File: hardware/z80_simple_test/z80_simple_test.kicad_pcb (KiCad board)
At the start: 2 copper layers, 95 x 100 mm, 38 parts, among them J2 Conn_02x15_Odd_Even, U1 Z84C000XPEG, U2 SRAM_512K8B_DIP_SOP_SOJ, U3 EEPROM_512K8B_DIP, U4 74XX138, U5 Z84C200XPEG, U6 Z84C200XPEG

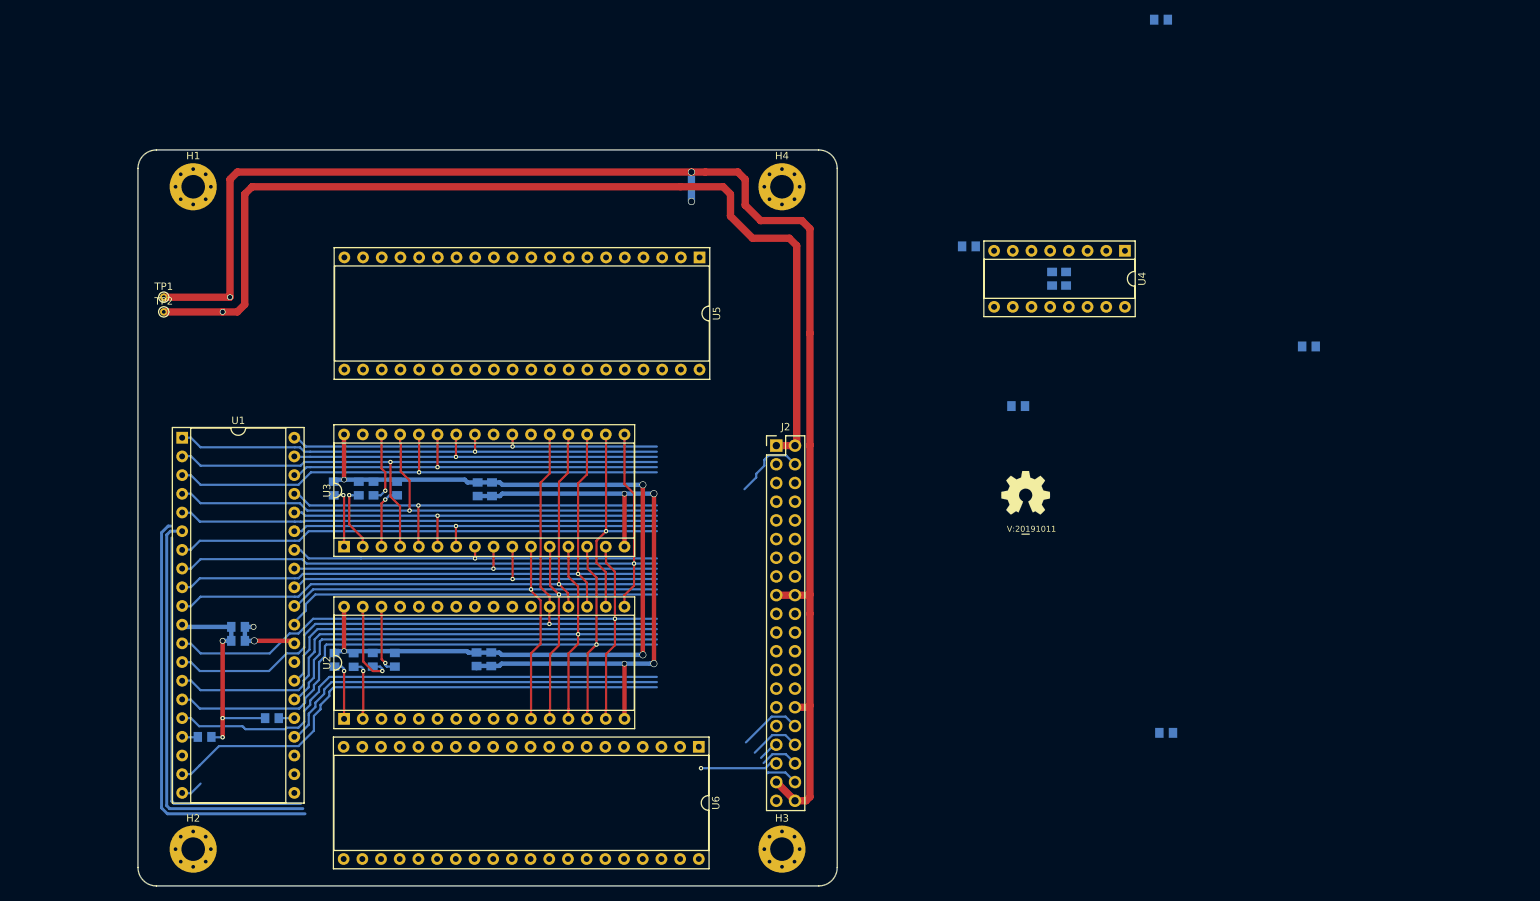
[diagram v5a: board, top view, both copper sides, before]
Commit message: after a bunch of false starts, this bus setup seems workable
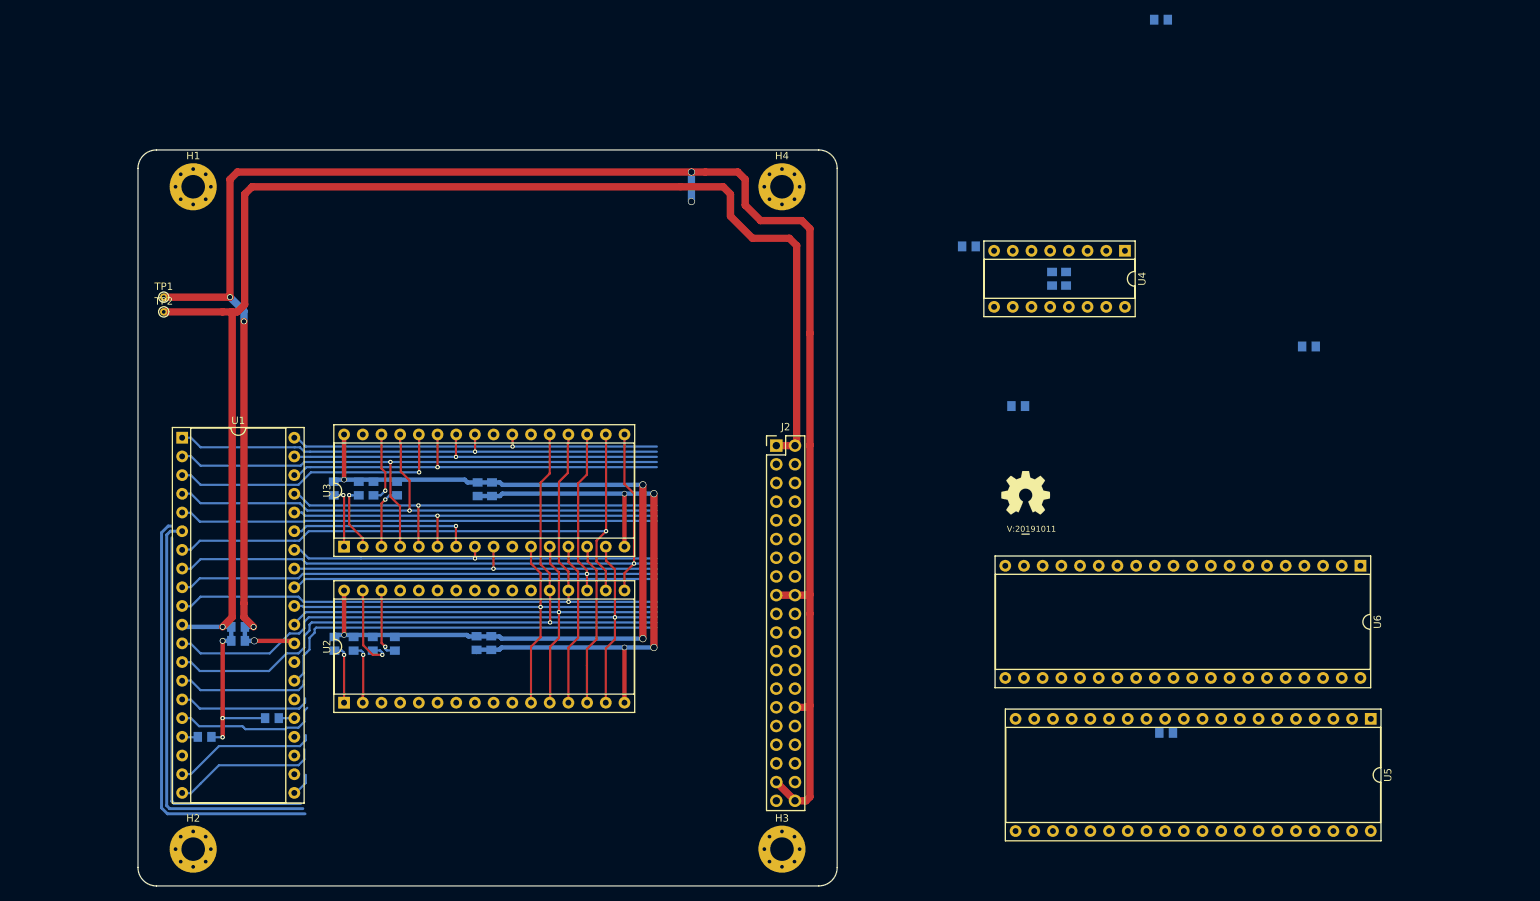
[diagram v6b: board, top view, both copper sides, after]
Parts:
- moved U5 110.7 mm to (270.0, 127.3)
- moved U6 93.2 mm to (268.6, 106.5)
- moved C3 2.20 mm to (148.5, 117.0)
- moved C4 2.20 mm to (150.5, 117.0)
- moved R4 2.20 mm to (131.8, 117.1)
- moved U2 2.20 mm to (130.5, 125.1)
- moved R5 2.18 mm to (129.2, 117.1)
- moved R6 2.18 mm to (137.4, 117.1)
- moved R7 2.18 mm to (134.4, 117.1)
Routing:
- net /!RESET: track 64.0 -> 0.30 mm
- net /!MREQ: track 78.3 -> 19.4 mm
- net /!WAIT: track 56.7 -> 0.32 mm
- net /D1: track 96.0 -> 40.4 mm, vias 1 -> 0
- net /D0: track 95.4 -> 40.2 mm, vias 1 -> 0
- net /!INT: track 69.6 -> 19.7 mm
- net /VSS: track 412.3 -> 456.2 mm, vias 9 -> 10
- net /VDD: track 286.9 -> 328.1 mm
- net /A13: track 70.9 -> 38.6 mm
- net /A5: track 52.4 -> 25.1 mm
- net /A15: track 75.1 -> 65.1 mm
- net /D4: track 90.0 -> 80.9 mm
- net /!IORQ: track 13.6 -> 19.9 mm, vias 1 -> 0
- net /!WR: track 5.82 -> 1.18 mm
- net /A2: track 54.1 -> 49.8 mm, vias 1 -> 0
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
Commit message: added zilog SIO to schematic and PCB
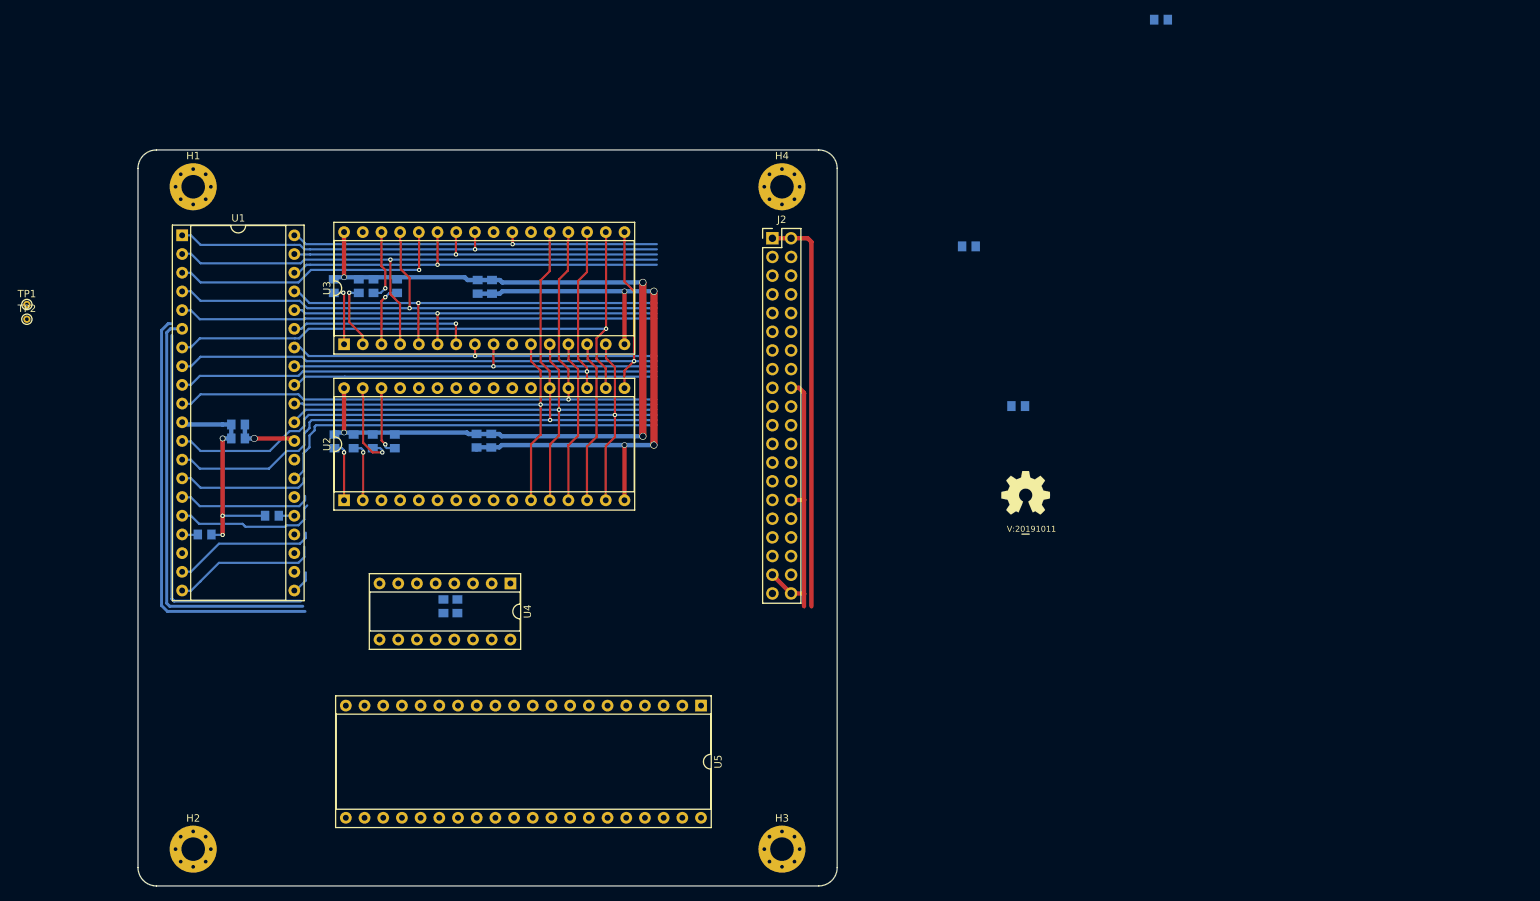
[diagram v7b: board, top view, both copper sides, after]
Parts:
- removed C11: 100n, SquantorRcl:C_0805+0603
- removed C12: 1u, SquantorRcl:C_0805+0603
- removed U6: Z84C200XPEG, Package_DIP:DIP-40_W15.24mm_Socket
- U5: value Z84C200XPEG -> Z84C40XPEG
- moved U4 94.9 mm to (153.1, 108.9)
- moved C7 93.9 mm to (144.0, 112.0)
- moved C8 93.9 mm to (145.9, 112.0)
- moved U5 91.0 mm to (179.0, 125.5)
- moved J2 28.2 mm to (188.7, 62.0)
- moved C1 27.5 mm to (116.1, 87.3)
- moved C2 27.5 mm to (116.1, 89.2)
- moved C3 27.5 mm to (148.5, 89.5)
- moved C4 27.5 mm to (150.5, 89.5)
- moved C5 27.5 mm to (150.6, 68.6)
- moved C6 27.5 mm to (148.7, 68.6)
- moved R1 27.5 mm to (120.7, 99.7)
- moved R10 27.5 mm to (134.5, 68.5)
- moved R11 27.5 mm to (129.1, 68.5)
- moved R3 27.5 mm to (111.5, 102.2)
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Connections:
- J2 pad 17: /VSS -> /A1
- J2 pad 19: /A0 -> /D7
- J2 pad 20: /A1 -> /A0
- J2 pad 21: /D6 -> /D5
- J2 pad 22: /D7 -> /D6
- J2 pad 23: /D4 -> /D3
- J2 pad 24: /D5 -> /D4
- J2 pad 25: /D2 -> /D1
- J2 pad 26: /D3 -> /D2
- J2 pad 27: /D0 -> /!IEI
- J2 pad 28: /D1 -> /D0
- U4 pad 14: (no net) -> /SEL_SIO
- U5 pad 1: /D2 -> /D1
- U5 pad 11: /VSS -> (no net)
- U5 pad 19: /D0 -> (no net)
- U5 pad 2: /D7 -> /D3
- U5 pad 20: /D1 -> /MCLK
- U5 pad 21: (no net) -> /!RESET
- U5 pad 23: /!INT -> (no net)
- U5 pad 25: /MCLK -> (no net)
- U5 pad 26: /VDD -> (no net)
- U5 pad 3: /D6 -> /D5
- U5 pad 31: (no net) -> /VSS
- U5 pad 32: (no net) -> /!RD
- U5 pad 33: (no net) -> /A1
- U5 pad 34: (no net) -> /A0
- U5 pad 35: /!RD -> /SEL_SIO
- U5 pad 37: /!M1 -> /D6
- U5 pad 38: /D5 -> /D4
- U5 pad 39: /D4 -> /D2
- U5 pad 4: /SEL_PIO -> /D7
- U5 pad 40: /D3 -> /D0
- U5 pad 5: /A1 -> /!INT
- U5 pad 6: /A0 -> /!IEI
- U5 pad 8: (no net) -> /!M1
- U5 pad 9: (no net) -> /VDD
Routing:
- net /VSS: track 456.2 -> 243.3 mm, vias 10 -> 5
- net /VDD: track 328.1 -> 203.0 mm, vias 8 -> 7

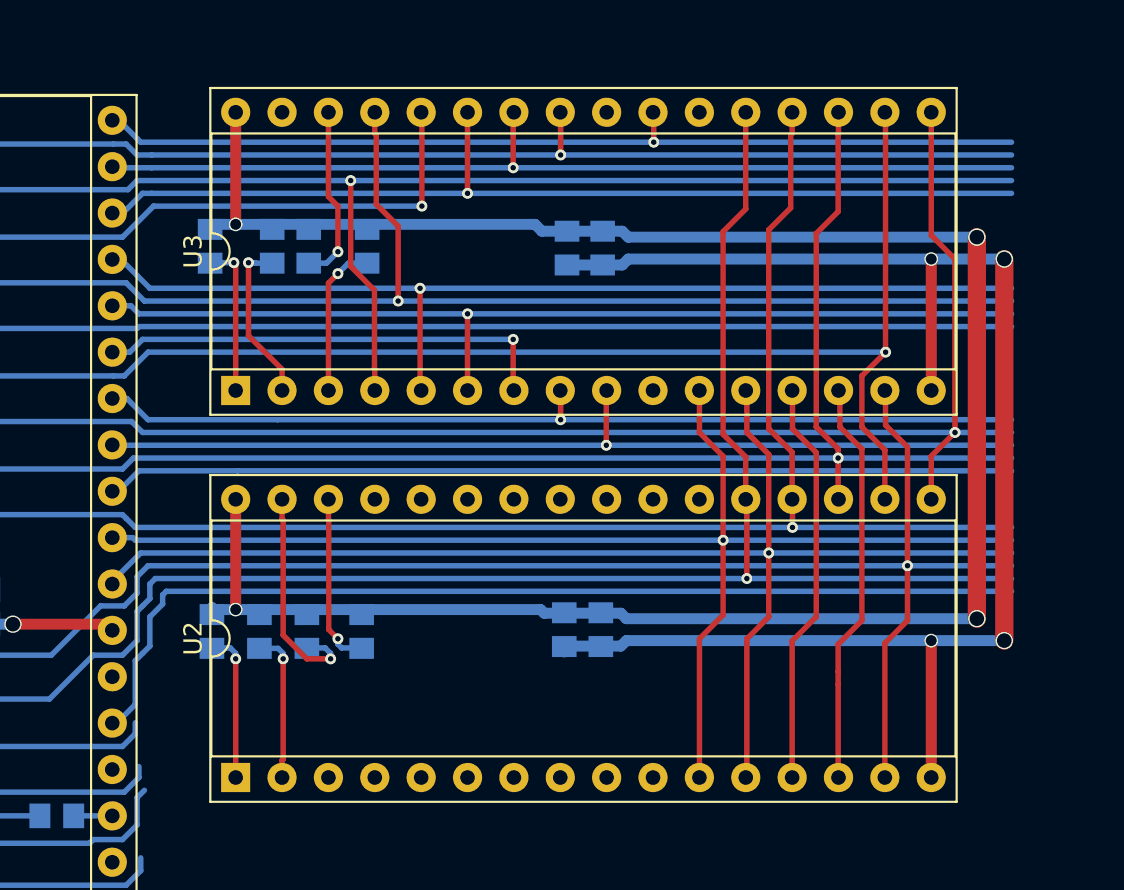
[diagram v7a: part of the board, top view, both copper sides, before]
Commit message: routed bus under memory chips
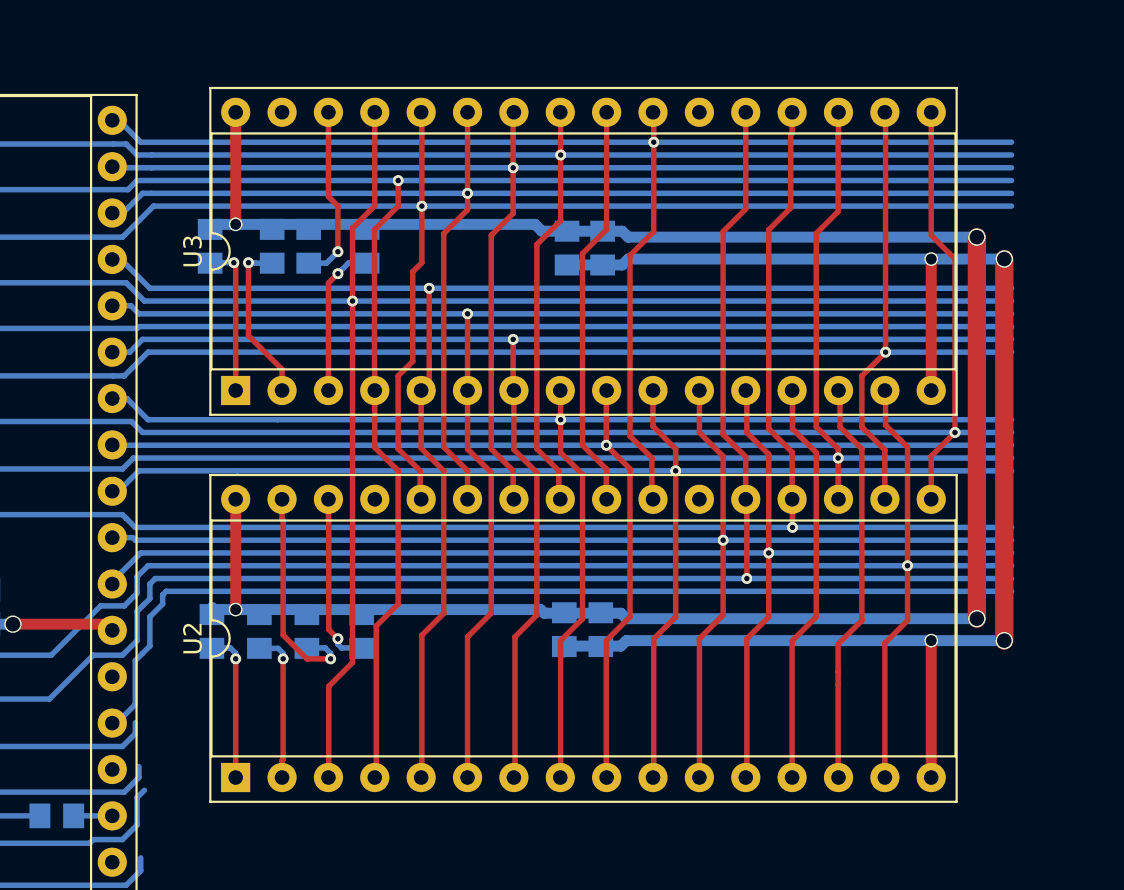
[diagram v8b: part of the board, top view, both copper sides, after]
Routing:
- net /A5: track 25.1 -> 74.6 mm
- net /A13: track 38.6 -> 88.0 mm
- net /A14: track 76.3 -> 103.0 mm
- net /A7: track 55.5 -> 77.9 mm
- net /!MEM_RD: track 0.00 -> 22.3 mm
- net /A6: track 53.7 -> 76.0 mm
- net /A12: track 77.3 -> 99.6 mm
- net /A2: track 49.8 -> 72.0 mm, vias 0 -> 1
- net /A10: track 51.4 -> 72.0 mm
- net /A4: track 51.5 -> 72.2 mm
- net /A11: track 67.6 -> 87.6 mm
- net /A3: track 52.3 -> 71.6 mm
- net /A9: track 52.3 -> 71.5 mm
- net /A8: track 54.1 -> 72.0 mm
- net /D4: track 80.9 -> 87.8 mm
